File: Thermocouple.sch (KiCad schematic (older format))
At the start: 14 parts

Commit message: Added footprints for the relay module, preliminarily annotated schematic, relay components placed on PCB
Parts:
- gave numbers to parts that had none: 12
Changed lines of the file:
@@
 CS_N
 $Comp
-L LM324 U?
-U 1 1 52F01AA7
+L LM324 U11
+U 2 1 52F01AA7
 P 7700 1900
-F 0 "U?" H 7750 2100 60  0000 C CNN
+F 0 "U11" H 7750 2100 60  0000 C CNN
 F 1 "LM324" H 7850 1700 50  0000 C CNN
 F 2 "" H 7700 1900 60  0000 C CNN
 F 3 "" H 7700 1900 60  0000 C CNN
-	1    7700 1900
+	2    7700 1900
 	-1   0    0    -1
 $EndComp
 $Comp
-L LM324 U?
-U 1 1 52F01AB9
+L LM324 U11
+U 3 1 52F01AB9
 P 7700 4100
-F 0 "U?" H 7750 4300 60  0000 C CNN
+F 0 "U11" H 7750 4300 60  0000 C CNN
 F 1 "LM324" H 7850 3900 50  0000 C CNN
 F 2 "" H 7700 4100 60  0000 C CNN
 F 3 "" H 7700 4100 60  0000 C CNN
-	1    7700 4100
-	-1   0    0    1
-$EndComp
-$Comp
-L LM324 U?
-U 1 1 52F01AC4
+	3    7700 4100
+	-1   0    0    1
+$EndComp
+$Comp
+L LM324 U7
+U 4 1 52F01AC4
 P 5200 3000
-F 0 "U?" H 5250 3200 60  0000 C CNN
+F 0 "U7" H 5250 3200 60  0000 C CNN
 F 1 "LM324" H 5350 2800 50  0000 C CNN
 F 2 "" H 5200 3000 60  0000 C CNN
 F 3 "" H 5200 3000 60  0000 C CNN
-	1    5200 3000
-	-1   0    0    1
-$EndComp
-$Comp
-L LM324 U?
+	4    5200 3000
+	-1   0    0    1
+$EndComp
+$Comp
+L LM324 U11
 U 1 1 52F01ACF
 P 7200 5500
-F 0 "U?" H 7250 5700 60  0000 C CNN
+F 0 "U11" H 7250 5700 60  0000 C CNN
 F 1 "LM324" H 7350 5300 50  0000 C CNN
 F 2 "" H 7200 5500 60  0000 C CNN
@@
 $EndComp
 $Comp
-L R R?
+L R R26
 U 1 1 52F01B4D
 P 6900 3000
-F 0 "R?" V 6980 3000 40  0000 C CNN
+F 0 "R26" V 6980 3000 40  0000 C CNN
 F 1 "R" V 6907 3001 40  0000 C CNN
 F 2 "" V 6830 3000 30  0000 C CNN
@@
 $EndComp
 $Comp
-L R R?
+L R R25
 U 1 1 52F01B58
 P 6900 2250
-F 0 "R?" V 6980 2250 40  0000 C CNN
+F 0 "R25" V 6980 2250 40  0000 C CNN
 F 1 "R" V 6907 2251 40  0000 C CNN
 F 2 "" V 6830 2250 30  0000 C CNN
@@
 $EndComp
 $Comp
-L R R?
+L R R27
 U 1 1 52F01B63
 P 6900 3750
-F 0 "R?" V 6980 3750 40  0000 C CNN
+F 0 "R27" V 6980 3750 40  0000 C CNN
 F 1 "R" V 6907 3751 40  0000 C CNN
 F 2 "" V 6830 3750 30  0000 C CNN
@@
 $EndComp
 $Comp
-L R R?
+L R R23
 U 1 1 52F01B93
 P 6350 1900
-F 0 "R?" V 6430 1900 40  0000 C CNN
+F 0 "R23" V 6430 1900 40  0000 C CNN
 F 1 "R" V 6357 1901 40  0000 C CNN
 F 2 "" V 6280 1900 30  0000 C CNN
@@
 $EndComp
 $Comp
-L R R?
+L R R21
 U 1 1 52F01B9E
 P 4950 1900
-F 0 "R?" V 5030 1900 40  0000 C CNN
+F 0 "R21" V 5030 1900 40  0000 C CNN
 F 1 "R" V 4957 1901 40  0000 C CNN
 F 2 "" V 4880 1900 30  0000 C CNN
@@
 $EndComp
 $Comp
-L R R?
+L R R24
 U 1 1 52F01BA9
 P 6350 4100
-F 0 "R?" V 6430 4100 40  0000 C CNN
+F 0 "R24" V 6430 4100 40  0000 C CNN
 F 1 "R" V 6357 4101 40  0000 C CNN
 F 2 "" V 6280 4100 30  0000 C CNN
@@
 $EndComp
 $Comp
-L R R?
+L R R22
 U 1 1 52F01BB4
 P 4950 4100
-F 0 "R?" V 5030 4100 40  0000 C CNN
+F 0 "R22" V 5030 4100 40  0000 C CNN
 F 1 "R" V 4957 4101 40  0000 C CNN
 F 2 "" V 4880 4100 30  0000 C CNN
@@
 $EndComp
 $Comp
-L -12V #PWR?
+L -12V #PWR45
 U 1 1 52F01D61
 P 5300 2500
-F 0 "#PWR?" H 5300 2630 20  0001 C CNN
+F 0 "#PWR45" H 5300 2630 20  0001 C CNN
 F 1 "-12V" H 5300 2600 30  0000 C CNN
 F 2 "" H 5300 2500 60  0000 C CNN
@@
 $EndComp
 $Comp
-L -12V #PWR?
+L -12V #PWR48
 U 1 1 52F01D73
 P 7800 2400
-F 0 "#PWR?" H 7800 2530 20  0001 C CNN
+F 0 "#PWR48" H 7800 2530 20  0001 C CNN
 F 1 "-12V" H 7800 2500 30  0000 C CNN
 F 2 "" H 7800 2400 60  0000 C CNN
@@
 $EndComp
 $Comp
-L -12V #PWR?
+L -12V #PWR49
 U 1 1 52F01D7E
 P 7800 3600
-F 0 "#PWR?" H 7800 3730 20  0001 C CNN
+F 0 "#PWR49" H 7800 3730 20  0001 C CNN
 F 1 "-12V" H 7800 3700 30  0000 C CNN
 F 2 "" H 7800 3600 60  0000 C CNN
@@
 $EndComp
 $Comp
-L +12V #PWR?
+L +12V #PWR46
 U 1 1 52F01E08
 P 5300 3500
-F 0 "#PWR?" H 5300 3450 20  0001 C CNN
+F 0 "#PWR46" H 5300 3450 20  0001 C CNN
 F 1 "+12V" H 5300 3600 30  0000 C CNN
 F 2 "" H 5300 3500 60  0000 C CNN
@@
 $EndComp
 $Comp
-L +12V #PWR?
+L +12V #PWR50
 U 1 1 52F01E29
 P 7800 4600
-F 0 "#PWR?" H 7800 4550 20  0001 C CNN
+F 0 "#PWR50" H 7800 4550 20  0001 C CNN
 F 1 "+12V" H 7800 4700 30  0000 C CNN
 F 2 "" H 7800 4600 60  0000 C CNN
@@
 $EndComp
 $Comp
-L +12V #PWR?
+L +12V #PWR47
 U 1 1 52F01E34
 P 7800 1400
-F 0 "#PWR?" H 7800 1350 20  0001 C CNN
+F 0 "#PWR47" H 7800 1350 20  0001 C CNN
 F 1 "+12V" H 7800 1500 30  0000 C CNN
 F 2 "" H 7800 1400 60  0000 C CNN
@@
 $EndComp
 $Comp
-L AGND #PWR?
+L AGND #PWR44
 U 1 1 52F01EB3
 P 4500 4300
-F 0 "#PWR?" H 4500 4300 40  0001 C CNN
+F 0 "#PWR44" H 4500 4300 40  0001 C CNN
 F 1 "AGND" H 4500 4230 50  0000 C CNN
 F 2 "" H 4500 4300 60  0000 C CNN
@@
 $EndComp
 $Comp
-L MCP3550-60-E/SN U?
+L MCP3550-60-E/SN U9
 U 1 1 52F01F2F
 P 2800 3150
-F 0 "U?" H 2250 3500 40  0000 C CNN
+F 0 "U9" H 2250 3500 40  0000 C CNN
 F 1 "MCP3550-60-E/SN" H 2500 3450 40  0000 C CNN
 F 2 "SO8" H 2600 3150 30  0000 C CIN
@@
 $EndComp
 $Comp
-L MCP3550-60-E/SN U?
+L MCP3550-60-E/SN U10
 U 1 1 52F02036
 P 2800 5650
-F 0 "U?" H 2250 6000 40  0000 C CNN
+F 0 "U10" H 2250 6000 40  0000 C CNN
 F 1 "MCP3550-60-E/SN" H 2500 5950 40  0000 C CNN
 F 2 "SO8" H 2600 5650 30  0000 C CIN
@@
 $EndComp
 $Comp
-L ZENER D?
+L ZENER D5
 U 1 1 52F02043
 P 8300 5800
-F 0 "D?" H 8300 5900 50  0000 C CNN
+F 0 "D5" H 8300 5900 50  0000 C CNN
 F 1 "ZENER" H 8300 5700 40  0000 C CNN
 F 2 "" H 8300 5800 60  0000 C CNN
@@
 $EndComp
 $Comp
-L +12V #PWR?
+L +12V #PWR51
 U 1 1 52F02055
 P 8300 5300
-F 0 "#PWR?" H 8300 5250 20  0001 C CNN
+F 0 "#PWR51" H 8300 5250 20  0001 C CNN
 F 1 "+12V" H 8300 5400 30  0000 C CNN
 F 2 "" H 8300 5300 60  0000 C CNN
@@
 $EndComp
 $Comp
-L AGND #PWR?
+L AGND #PWR52
 U 1 1 52F0208D
 P 8300 6300
-F 0 "#PWR?" H 8300 6300 40  0001 C CNN
+F 0 "#PWR52" H 8300 6300 40  0001 C CNN
 F 1 "AGND" H 8300 6230 50  0000 C CNN
 F 2 "" H 8300 6300 60  0000 C CNN
@@
 	3500 5800 3500 6000
 $Comp
-L AGND #PWR?
+L AGND #PWR43
 U 1 1 52F02222
 P 3500 6000
-F 0 "#PWR?" H 3500 6000 40  0001 C CNN
+F 0 "#PWR43" H 3500 6000 40  0001 C CNN
 F 1 "AGND" H 3500 5930 50  0000 C CNN
 F 2 "" H 3500 6000 60  0000 C CNN

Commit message: Associated and placed the thermocouple module
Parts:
- removed D5: ZENER, symbol ZENER
- removed U10, U9: MCP3550-60-E/SN, SO8, symbol MCP3550-60-E/SN
- removed unit 1 of U11
- added C10, C5, C6, C7, C8, C9: C, symbol C
- added P2: CONN_2, symbol CONN_2
- added P3: CONN_3X2, symbol CONN_3X2
- added R43, R44, R47, R48: R, symbol R
- added U10: LMT84, symbol LMT84
- added U9: MCP3901, symbol MCP3901
- U11: value LM324 -> OPA4170
- U11: renamed from U7; value LM324 -> OPA4170
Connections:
- net labels added: +5V, CH0+, CH0-, CH1+, CH1-, REF+, REF-, ~CS, ~DR, ~RESET
- net labels removed: CS_N
- wire segments 45 -> 89
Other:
- note added: "16-24bit ADC"
- note added: "Temperature Sensor"
- note removed: "General Temperature Sensor"
- moved on the sheet: R22, R24, R27

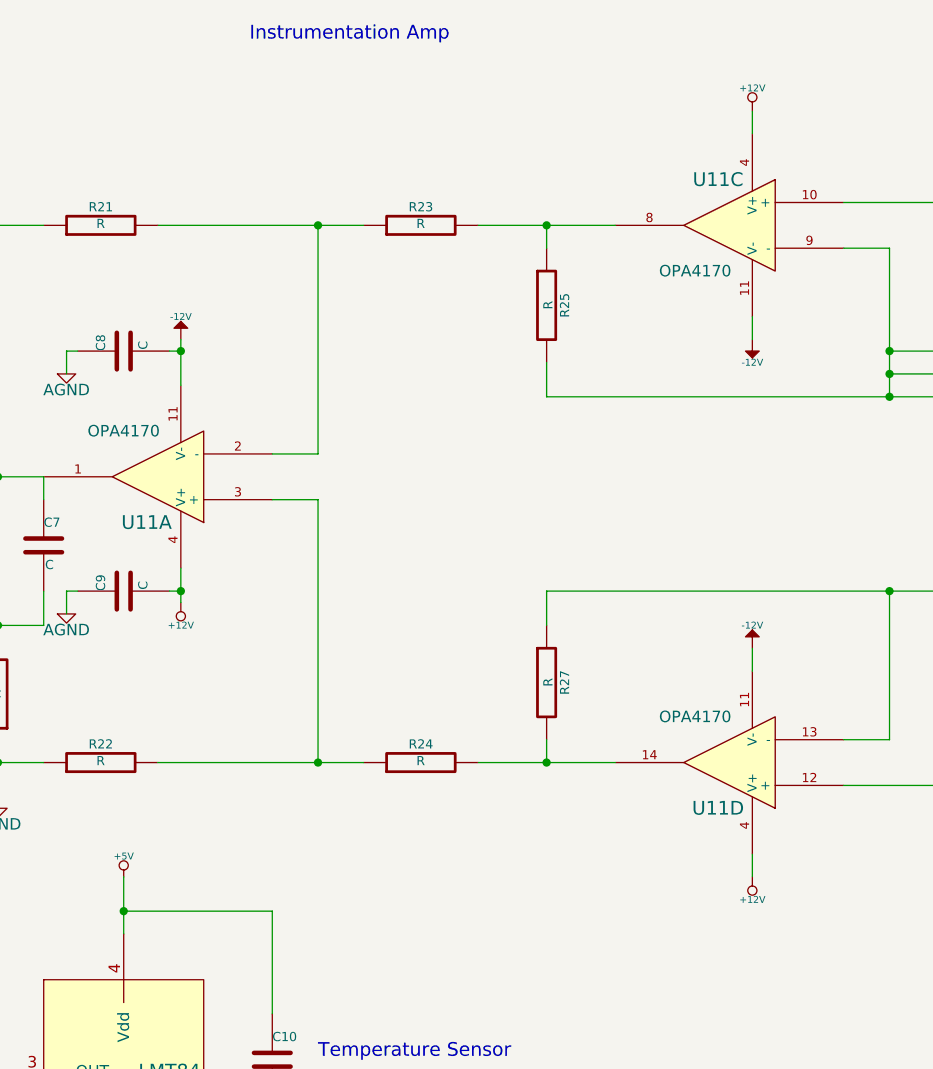
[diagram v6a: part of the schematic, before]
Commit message: Various minor updates after Ground and Power Planes video
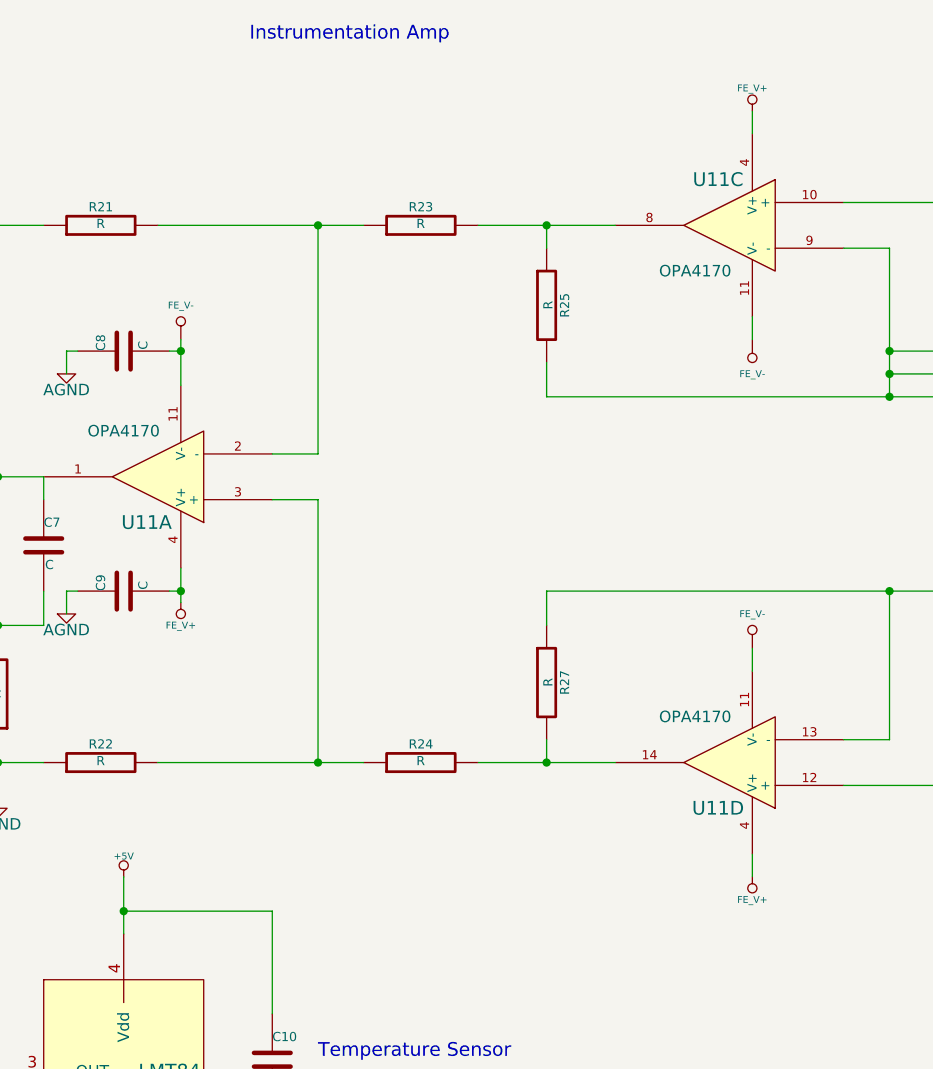
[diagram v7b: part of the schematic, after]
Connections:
- net +12V renamed FE_V+
- net -12V renamed FE_V-
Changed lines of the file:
@@
 $EndComp
 $Comp
-L -12V #PWR048
-U 1 1 52F01D61
-P 5300 2400
-F 0 "#PWR048" H 5300 2530 20  0001 C CNN
-F 1 "-12V" H 5300 2500 30  0000 C CNN
-F 2 "" H 5300 2400 60  0000 C CNN
-F 3 "" H 5300 2400 60  0000 C CNN
-	1    5300 2400
-	1    0    0    -1
-$EndComp
-$Comp
-L -12V #PWR049
-U 1 1 52F01D73
-P 7800 2400
-F 0 "#PWR049" H 7800 2530 20  0001 C CNN
-F 1 "-12V" H 7800 2500 30  0000 C CNN
-F 2 "" H 7800 2400 60  0000 C CNN
-F 3 "" H 7800 2400 60  0000 C CNN
-	1    7800 2400
-	-1   0    0    1
-$EndComp
-$Comp
-L -12V #PWR050
-U 1 1 52F01D7E
-P 7800 3750
-F 0 "#PWR050" H 7800 3880 20  0001 C CNN
-F 1 "-12V" H 7800 3850 30  0000 C CNN
-F 2 "" H 7800 3750 60  0000 C CNN
-F 3 "" H 7800 3750 60  0000 C CNN
-	1    7800 3750
-	1    0    0    -1
-$EndComp
-$Comp
-L +12V #PWR051
-U 1 1 52F01E08
-P 5300 3550
-F 0 "#PWR051" H 5300 3500 20  0001 C CNN
-F 1 "+12V" H 5300 3650 30  0000 C CNN
-F 2 "" H 5300 3550 60  0000 C CNN
-F 3 "" H 5300 3550 60  0000 C CNN
-	1    5300 3550
-	-1   0    0    1
-$EndComp
-$Comp
-L +12V #PWR052
-U 1 1 52F01E29
-P 7800 4750
-F 0 "#PWR052" H 7800 4700 20  0001 C CNN
-F 1 "+12V" H 7800 4850 30  0000 C CNN
-F 2 "" H 7800 4750 60  0000 C CNN
-F 3 "" H 7800 4750 60  0000 C CNN
-	1    7800 4750
-	-1   0    0    1
-$EndComp
-$Comp
-L +12V #PWR053
-U 1 1 52F01E34
-P 7800 1400
-F 0 "#PWR053" H 7800 1350 20  0001 C CNN
-F 1 "+12V" H 7800 1500 30  0000 C CNN
-F 2 "" H 7800 1400 60  0000 C CNN
-F 3 "" H 7800 1400 60  0000 C CNN
-	1    7800 1400
-	1    0    0    -1
-$EndComp
-$Comp
-L AGND #PWR054
+L AGND #PWR57
 U 1 1 52F01EB3
 P 4500 4450
-F 0 "#PWR054" H 4500 4450 40  0001 C CNN
+F 0 "#PWR57" H 4500 4450 40  0001 C CNN
 F 1 "AGND" H 4500 4380 50  0000 C CNN
 F 2 "" H 4500 4450 60  0000 C CNN
@@
 $EndComp
 $Comp
-L AGND #PWR055
+L AGND #PWR56
 U 1 1 53054233
 P 4200 6450
-F 0 "#PWR055" H 4200 6450 40  0001 C CNN
+F 0 "#PWR56" H 4200 6450 40  0001 C CNN
 F 1 "AGND" H 4200 6380 50  0000 C CNN
 F 2 "" H 4200 6450 60  0000 C CNN
@@
 $EndComp
 $Comp
-L +5V #PWR056
+L +5V #PWR60
 U 1 1 530546E7
 P 5050 4750
-F 0 "#PWR056" H 5050 4840 20  0001 C CNN
+F 0 "#PWR60" H 5050 4840 20  0001 C CNN
 F 1 "+5V" H 5050 4840 30  0000 C CNN
 F 2 "" H 5050 4750 60  0000 C CNN
@@
 $EndComp
 $Comp
-L AGND #PWR057
+L AGND #PWR58
 U 1 1 530549E4
 P 4800 2550
-F 0 "#PWR057" H 4800 2550 40  0001 C CNN
+F 0 "#PWR58" H 4800 2550 40  0001 C CNN
 F 1 "AGND" H 4800 2480 50  0000 C CNN
 F 2 "" H 4800 2550 60  0000 C CNN
@@
 $EndComp
 $Comp
-L AGND #PWR058
+L AGND #PWR59
 U 1 1 53054AA0
 P 4800 3600
-F 0 "#PWR058" H 4800 3600 40  0001 C CNN
+F 0 "#PWR59" H 4800 3600 40  0001 C CNN
 F 1 "AGND" H 4800 3530 50  0000 C CNN
 F 2 "" H 4800 3600 60  0000 C CNN
@@
 $EndComp
 $Comp
-L +5V #PWR059
+L +5V #PWR53
 U 1 1 53054B2C
 P 3100 1500
-F 0 "#PWR059" H 3100 1590 20  0001 C CNN
+F 0 "#PWR53" H 3100 1590 20  0001 C CNN
 F 1 "+5V" H 3100 1590 30  0000 C CNN
 F 2 "" H 3100 1500 60  0000 C CNN
@@
 $EndComp
 $Comp
-L AGND #PWR060
+L AGND #PWR55
 U 1 1 53054C58
 P 3600 1750
-F 0 "#PWR060" H 3600 1750 40  0001 C CNN
+F 0 "#PWR55" H 3600 1750 40  0001 C CNN
 F 1 "AGND" H 3600 1680 50  0000 C CNN
 F 2 "" H 3600 1750 60  0000 C CNN
@@
 $EndComp
 $Comp
-L AGND #PWR061
+L AGND #PWR54
 U 1 1 5305505B
 P 3100 4050
-F 0 "#PWR061" H 3100 4050 40  0001 C CNN
+F 0 "#PWR54" H 3100 4050 40  0001 C CNN
 F 1 "AGND" H 3100 3980 50  0000 C CNN
 F 2 "" H 3100 4050 60  0000 C CNN
@@
 $EndComp
 $Comp
-L AGND #PWR062
+L AGND #PWR52
 U 1 1 5305533E
 P 2500 4050
-F 0 "#PWR062" H 2500 4050 40  0001 C CNN
+F 0 "#PWR52" H 2500 4050 40  0001 C CNN
 F 1 "AGND" H 2500 3980 50  0000 C CNN
 F 2 "" H 2500 4050 60  0000 C CNN
@@
 $EndComp
 $Comp
-L +5V #PWR063
+L +5V #PWR51
 U 1 1 53055345
 P 2500 1500
-F 0 "#PWR063" H 2500 1590 20  0001 C CNN
+F 0 "#PWR51" H 2500 1590 20  0001 C CNN
 F 1 "+5V" H 2500 1590 30  0000 C CNN
 F 2 "" H 2500 1500 60  0000 C CNN
@@
 $EndComp
 $Comp
-L AGND #PWR064
+L AGND #PWR50
 U 1 1 53055353
 P 2000 1750
-F 0 "#PWR064" H 2000 1750 40  0001 C CNN
+F 0 "#PWR50" H 2000 1750 40  0001 C CNN
 F 1 "AGND" H 2000 1680 50  0000 C CNN
 F 2 "" H 2000 1750 60  0000 C CNN
@@
 Wire Wire Line
 	1050 3050 1700 3050
+$Comp
+L FE_V+ #PWR66
+U 1 1 530BD56D
+P 7800 4750
+F 0 "#PWR66" H 7800 4850 30  0001 C CNN
+F 1 "FE_V+" H 7800 4850 30  0000 C CNN
+F 2 "" H 7800 4750 60  0000 C CNN
+F 3 "" H 7800 4750 60  0000 C CNN
+	1    7800 4750
+	-1   0    0    1
+$EndComp
+$Comp
+L FE_V+ #PWR62
+U 1 1 530BD573
+P 5300 3550
+F 0 "#PWR62" H 5300 3650 30  0001 C CNN
+F 1 "FE_V+" H 5300 3650 30  0000 C CNN
+F 2 "" H 5300 3550 60  0000 C CNN
+F 3 "" H 5300 3550 60  0000 C CNN
+	1    5300 3550
+	-1   0    0    1
+$EndComp
+$Comp
+L FE_V- #PWR61
+U 1 1 530BD604
+P 5300 2400
+F 0 "#PWR61" H 5300 2600 40  0001 C CNN
+F 1 "FE_V-" H 5300 2550 30  0000 C CNN
+F 2 "" H 5300 2400 60  0000 C CNN
+F 3 "" H 5300 2400 60  0000 C CNN
+	1    5300 2400
+	1    0    0    -1
+$EndComp
+$Comp
+L FE_V+ #PWR63
+U 1 1 530BD635
+P 7800 1400
+F 0 "#PWR63" H 7800 1500 30  0001 C CNN
+F 1 "FE_V+" H 7800 1500 30  0000 C CNN
+F 2 "" H 7800 1400 60  0000 C CNN
+F 3 "" H 7800 1400 60  0000 C CNN
+	1    7800 1400
+	1    0    0    -1
+$EndComp
+$Comp
+L FE_V- #PWR64
+U 1 1 530BD640
+P 7800 2400
+F 0 "#PWR64" H 7800 2600 40  0001 C CNN
+F 1 "FE_V-" H 7800 2550 30  0000 C CNN
+F 2 "" H 7800 2400 60  0000 C CNN
+F 3 "" H 7800 2400 60  0000 C CNN
+	1    7800 2400
+	-1   0    0    1
+$EndComp
+$Comp
+L FE_V- #PWR65
+U 1 1 530BD64B
+P 7800 3750
+F 0 "#PWR65" H 7800 3950 40  0001 C CNN
+F 1 "FE_V-" H 7800 3900 30  0000 C CNN
+F 2 "" H 7800 3750 60  0000 C CNN
+F 3 "" H 7800 3750 60  0000 C CNN
+	1    7800 3750
+	1    0    0    -1
+$EndComp
 $EndSCHEMATC
